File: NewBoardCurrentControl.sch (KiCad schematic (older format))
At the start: 21 parts, among them Q401 RSR030N06TL, U401 ADA4528-2ACPZ-RL, U402 782853152_WE-CBA_08

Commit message: add footprints julia
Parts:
- Q401: footprint SOT95P280X100-3N -> footprint libraries:RSR030N06TL
- U401: footprint CP_8_11_ADI -> footprint libraries:ADA4528-2ACPZ-RL
- U402: footprint (none) -> footprint libraries:782853121
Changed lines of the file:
@@
 F 0 "U401" H 5300 3937 60  0000 C CNN
 F 1 "ADA4528-2ACPZ-RL" H 5300 3831 60  0000 C CNN
-F 2 "CP_8_11_ADI" H 5300 3790 60  0001 C CNN
+F 2 "footprint libraries:ADA4528-2ACPZ-RL" H 5300 3790 60  0001 C CNN
 F 3 "" H 4500 3550 60  0000 C CNN
 	1    4500 3550
@@
 F 0 "Q401" H 7400 4615 50  0000 C CNN
 F 1 "RSR030N06TL" H 7400 4524 50  0000 C CNN
-F 2 "SOT95P280X100-3N" H 7900 4450 50  0001 L CNN
+F 2 "footprint libraries:RSR030N06TL" H 7900 4450 50  0001 L CNN
 F 3 "https://componentsearchengine.com/Datasheets/2/RSR030N06TL.pdf" H 7900 4350 50  0001 L CNN
 F 4 "Rohm, MOSFET, RSR030N06TL ROHM RSR030N06TL N-channel MOSFET Transistor, 3 A, 60 V, 3-Pin SC-96" H 7900 4250 50  0001 L CNN "Description"
@@
 F 0 "U402" V 7979 3528 50  0000 L CNN
 F 1 "782853152_WE-CBA_08" V 8070 3528 50  0000 L CNN
-F 2 "" H 8150 3400 50  0001 C CNN
+F 2 "footprint libraries:782853121" H 8150 3400 50  0001 C CNN
 F 3 "" H 8150 3400 50  0001 C CNN
 	1    8050 3400

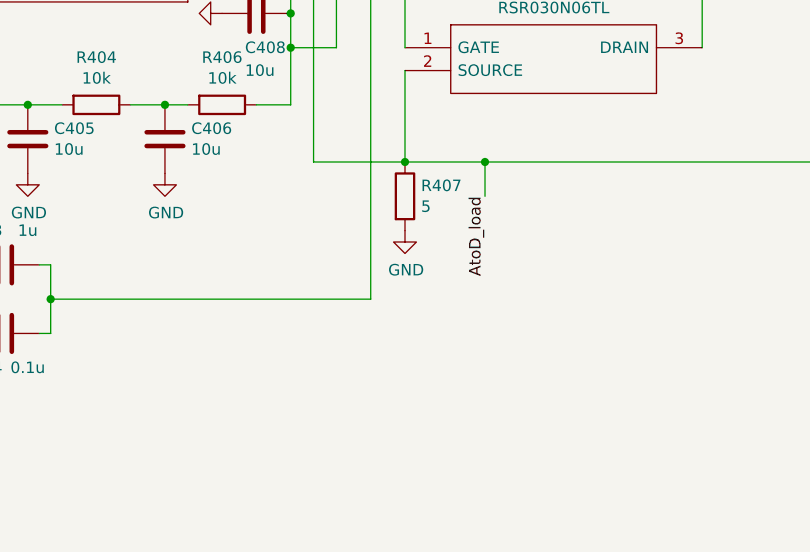
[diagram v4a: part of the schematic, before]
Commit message: added vishay dude & capacitor & resistor footprints
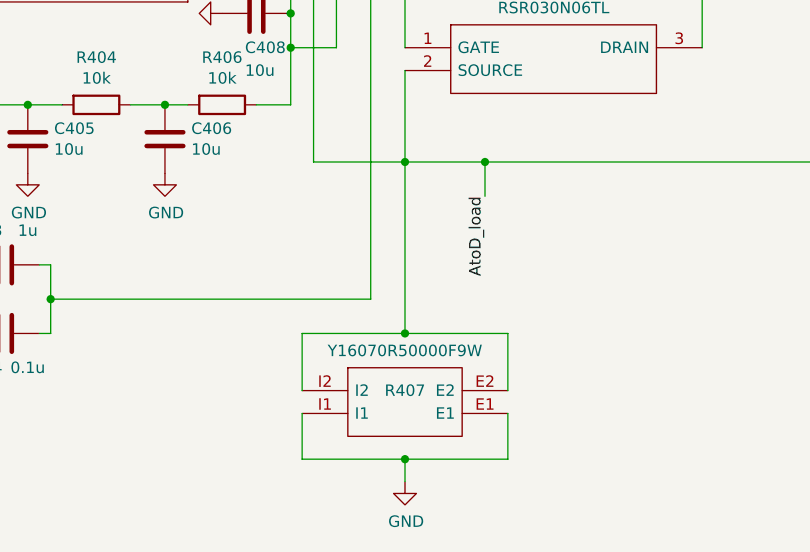
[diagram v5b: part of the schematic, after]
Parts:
- removed R407: 5, symbol Device:R
- added R407: Y16070R50000F9W, Y16072R00000T9W, symbol Y16070R50000F9W:Y16070R50000F9W
- C401, C402, C403, C404, C405, C406, C407, C408, C409, C410, C411: footprint (none) -> Capacitor_SMD:C_0402_1005Metric
- R401, R402, R405: footprint (none) -> Resistor_SMD:R_0402_1005Metric
- R403, R404, R406: footprint (none) -> Resistor_SMD:R_0603_1608Metric
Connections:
- net AtoD_load: now also R407.E2, R407.I2
- net GND: now also R407.E1, R407.I1
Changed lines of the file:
@@
 F 0 "C410" H 7615 2796 50  0000 L CNN
 F 1 "10u" H 7615 2705 50  0000 L CNN
-F 2 "" H 7538 2600 50  0001 C CNN
+F 2 "Capacitor_SMD:C_0402_1005Metric" H 7538 2600 50  0001 C CNN
 F 3 "~" H 7500 2750 50  0001 C CNN
 	1    7500 2750
@@
 F 0 "C411" H 9465 2796 50  0000 L CNN
 F 1 "10u" H 9465 2705 50  0000 L CNN
-F 2 "" H 9388 2600 50  0001 C CNN
+F 2 "Capacitor_SMD:C_0402_1005Metric" H 9388 2600 50  0001 C CNN
 F 3 "~" H 9350 2750 50  0001 C CNN
 	1    9350 2750
@@
 Connection ~ 6750 4850
 $Comp
-L Device:R R407
-U 1 1 60C96966
-P 6750 5000
-F 0 "R407" H 6820 5046 50  0000 L CNN
-F 1 "5" H 6820 4955 50  0000 L CNN
-F 2 "" V 6680 5000 50  0001 C CNN
-F 3 "~" H 6750 5000 50  0001 C CNN
-	1    6750 5000
-	1    0    0    -1
-$EndComp
-$Comp
 L power:GND #PWR0407
 U 1 1 60C97896
-P 6750 5150
-F 0 "#PWR0407" H 6750 4900 50  0001 C CNN
-F 1 "GND" H 6755 4977 50  0000 C CNN
-F 2 "" H 6750 5150 50  0001 C CNN
-F 3 "" H 6750 5150 50  0001 C CNN
-	1    6750 5150
+P 6750 6250
+F 0 "#PWR0407" H 6750 6000 50  0001 C CNN
+F 1 "GND" H 6755 6077 50  0000 C CNN
+F 2 "" H 6750 6250 50  0001 C CNN
+F 3 "" H 6750 6250 50  0001 C CNN
+	1    6750 6250
 	1    0    0    -1
 $EndComp
@@
 F 0 "R406" V 5743 4600 50  0000 C CNN
 F 1 "10k" V 5834 4600 50  0000 C CNN
-F 2 "" V 5880 4600 50  0001 C CNN
+F 2 "Resistor_SMD:R_0603_1608Metric" V 5880 4600 50  0001 C CNN
 F 3 "~" H 5950 4600 50  0001 C CNN
 	1    5950 4600
@@
 F 0 "C406" H 5815 4796 50  0000 L CNN
 F 1 "10u" H 5815 4705 50  0000 L CNN
-F 2 "" H 5738 4600 50  0001 C CNN
+F 2 "Capacitor_SMD:C_0402_1005Metric" H 5738 4600 50  0001 C CNN
 F 3 "~" H 5700 4750 50  0001 C CNN
 	1    5700 4750
@@
 F 0 "R404" V 5193 4600 50  0000 C CNN
 F 1 "10k" V 5284 4600 50  0000 C CNN
-F 2 "" V 5330 4600 50  0001 C CNN
+F 2 "Resistor_SMD:R_0603_1608Metric" V 5330 4600 50  0001 C CNN
 F 3 "~" H 5400 4600 50  0001 C CNN
 	1    5400 4600
@@
 F 0 "C405" H 5215 4796 50  0000 L CNN
 F 1 "10u" H 5215 4705 50  0000 L CNN
-F 2 "" H 5138 4600 50  0001 C CNN
+F 2 "Capacitor_SMD:C_0402_1005Metric" H 5138 4600 50  0001 C CNN
 F 3 "~" H 5100 4750 50  0001 C CNN
 	1    5100 4750
@@
 F 0 "R403" V 4593 4600 50  0000 C CNN
 F 1 "10k" V 4684 4600 50  0000 C CNN
-F 2 "" V 4730 4600 50  0001 C CNN
+F 2 "Resistor_SMD:R_0603_1608Metric" V 4730 4600 50  0001 C CNN
 F 3 "~" H 4800 4600 50  0001 C CNN
 	1    4800 4600
@@
 F 0 "C408" V 6250 4150 50  0000 L CNN
 F 1 "10u" V 6350 4150 50  0000 L CNN
-F 2 "" H 6138 4050 50  0001 C CNN
+F 2 "Capacitor_SMD:C_0402_1005Metric" H 6138 4050 50  0001 C CNN
 F 3 "~" H 6100 4200 50  0001 C CNN
 	1    6100 4200
@@
 F 0 "R401" V 3843 3650 50  0000 C CNN
 F 1 "1k" V 3934 3650 50  0000 C CNN
-F 2 "" V 3980 3650 50  0001 C CNN
+F 2 "Resistor_SMD:R_0402_1005Metric" V 3980 3650 50  0001 C CNN
 F 3 "~" H 4050 3650 50  0001 C CNN
 	1    4050 3650
@@
 F 0 "C401" V 3498 3650 50  0000 C CNN
 F 1 "1u" V 3589 3650 50  0000 C CNN
-F 2 "" H 3788 3500 50  0001 C CNN
+F 2 "Capacitor_SMD:C_0402_1005Metric" H 3788 3500 50  0001 C CNN
 F 3 "~" H 3750 3650 50  0001 C CNN
 	1    3750 3650
@@
 F 0 "R402" V 4557 3400 50  0000 C CNN
 F 1 "1k" V 4466 3400 50  0000 C CNN
-F 2 "" V 4280 3400 50  0001 C CNN
+F 2 "Resistor_SMD:R_0402_1005Metric" V 4280 3400 50  0001 C CNN
 F 3 "~" H 4350 3400 50  0001 C CNN
 	1    4350 3400
@@
 F 0 "C407" H 6015 2746 50  0000 L CNN
 F 1 "0.1u" H 6015 2655 50  0000 L CNN
-F 2 "" H 5938 2550 50  0001 C CNN
+F 2 "Capacitor_SMD:C_0402_1005Metric" H 5938 2550 50  0001 C CNN
 F 3 "~" H 5900 2700 50  0001 C CNN
 	1    5900 2700
@@
 F 0 "R405" V 5707 2850 50  0000 C CNN
 F 1 "100" V 5616 2850 50  0000 C CNN
-F 2 "" V 5430 2850 50  0001 C CNN
+F 2 "Resistor_SMD:R_0402_1005Metric" V 5430 2850 50  0001 C CNN
 F 3 "~" H 5500 2850 50  0001 C CNN
 	1    5500 2850
@@
 F 0 "C409" H 6565 3246 50  0000 L CNN
 F 1 "1u" H 6565 3155 50  0000 L CNN
-F 2 "" H 6488 3050 50  0001 C CNN
+F 2 "Capacitor_SMD:C_0402_1005Metric" H 6488 3050 50  0001 C CNN
 F 3 "~" H 6450 3200 50  0001 C CNN
 	1    6450 3200
@@
 F 0 "C402" H 3735 4154 50  0000 R CNN
 F 1 "0.1u" H 3735 4245 50  0000 R CNN
-F 2 "" H 3888 4050 50  0001 C CNN
+F 2 "Capacitor_SMD:C_0402_1005Metric" H 3888 4050 50  0001 C CNN
 F 3 "~" H 3850 4200 50  0001 C CNN
 	1    3850 4200
@@
 F 0 "C403" V 4850 5200 50  0000 C CNN
 F 1 "1u" V 4850 5400 50  0000 C CNN
-F 2 "" H 5038 5150 50  0001 C CNN
+F 2 "Capacitor_SMD:C_0402_1005Metric" H 5038 5150 50  0001 C CNN
 F 3 "~" H 5000 5300 50  0001 C CNN
 	1    5000 5300
@@
 F 0 "C404" V 5150 5500 50  0000 C CNN
 F 1 "0.1u" V 5150 5700 50  0000 C CNN
-F 2 "" H 5038 5450 50  0001 C CNN
+F 2 "Capacitor_SMD:C_0402_1005Metric" H 5038 5450 50  0001 C CNN
 F 3 "~" H 5000 5600 50  0001 C CNN
 	1    5000 5600
@@
 Text Label 7650 1450 2    50   ~ 0
 V2_3.3V
+$Comp
+L Y16070R50000F9W:Y16070R50000F9W R407
+U 1 1 60D382BE
+P 6300 5850
+F 0 "R407" H 6750 5850 50  0000 C CNN
+F 1 "Y16070R50000F9W" H 6750 6024 50  0000 C CNN
+F 2 "Y16072R00000T9W" H 7050 5950 50  0001 L CNN
+F 3 "http://www.vishaypg.com/docs/63094/vcs1625z.pdf" H 7050 5850 50  0001 L CNN
+F 4 "Vishay Foil Resistors VCS Series Metal Foil Precision Surface Mount Fixed Resistor 500m +/-1% 0.5W +/-0.2ppm/C" H 7050 5750 50  0001 L CNN "Description"
+F 5 "1" H 7050 5650 50  0001 L CNN "Height"
+F 6 "Vishay" H 7050 5550 50  0001 L CNN "Manufacturer_Name"
+F 7 "Y16070R50000F9W" H 7050 5450 50  0001 L CNN "Manufacturer_Part_Number"
+F 8 "71-VCS1625Z0R5000FSW" H 7050 5350 50  0001 L CNN "Mouser Part Number"
+F 9 "https://www.mouser.co.uk/ProductDetail/Vishay-Precision-Group-Foil-Resistors/Y16070R50000F9W?qs=adduyb8LSTEElqj6iywYlw%3D%3D" H 7050 5250 50  0001 L CNN "Mouser Price/Stock"
+F 10 "Y16070R50000F9W" H 7050 5150 50  0001 L CNN "Arrow Part Number"
+F 11 "https://www.arrow.com/en/products/y16070r50000f9w/vishay-precision-group" H 7050 5050 50  0001 L CNN "Arrow Price/Stock"
+	1    6300 5850
+	1    0    0    -1
+$EndComp
+Wire Wire Line
+	6750 5600 6300 5600
+Wire Wire Line
+	6300 5600 6300 5850
+Wire Wire Line
+	6750 4850 6750 5600
+Wire Wire Line
+	7200 5850 7200 5600
+Wire Wire Line
+	7200 5600 6750 5600
+Connection ~ 6750 5600
+Wire Wire Line
+	7200 5950 7200 6150
+Wire Wire Line
+	7200 6150 6750 6150
+Wire Wire Line
+	6750 6150 6750 6250
+Wire Wire Line
+	6750 6150 6300 6150
+Wire Wire Line
+	6300 6150 6300 5950
+Connection ~ 6750 6150
 $EndSCHEMATC

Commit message: changed all 'odd' resistors in thermal control footprints
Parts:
- R407: footprint Y16072R00000T9W -> footprint libraries:Y16072R00000T9W
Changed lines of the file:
@@
 F 0 "R407" H 6750 5850 50  0000 C CNN
 F 1 "Y16070R50000F9W" H 6750 6024 50  0000 C CNN
-F 2 "Y16072R00000T9W" H 7050 5950 50  0001 L CNN
+F 2 "footprint libraries:Y16072R00000T9W" H 7050 5950 50  0001 L CNN
 F 3 "http://www.vishaypg.com/docs/63094/vcs1625z.pdf" H 7050 5850 50  0001 L CNN
 F 4 "Vishay Foil Resistors VCS Series Metal Foil Precision Surface Mount Fixed Resistor 500m +/-1% 0.5W +/-0.2ppm/C" H 7050 5750 50  0001 L CNN "Description"

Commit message: changes on nano and laser
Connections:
- net V2_3.3V renamed Laser_3.3VPower_Supply
- net Laser_3.3VPower_Supply: no longer C410.2, U402.~
- new net To_Laser: C410.2, U402.~
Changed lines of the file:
@@
 	7500 2900 7500 3050
-Wire Wire Line
-	8050 2200 8050 3050
 Wire Wire Line
 	9350 2900 9350 3700
@@
 Text Label 4250 4200 0    50   ~ 0
 V5
-Connection ~ 8050 3050
 Connection ~ 8050 3700
 $Comp
@@
 	6300 6150 6300 5950
 Connection ~ 6750 6150
+Wire Wire Line
+	8050 2200 8050 2450
+Wire Wire Line
+	8050 2450 8500 2450
+Wire Wire Line
+	8500 2450 8500 1500
+Wire Wire Line
+	8500 1500 10500 1500
+Wire Wire Line
+	8050 3050 8050 2900
+Wire Wire Line
+	8050 2900 8850 2900
+Wire Wire Line
+	8850 2900 8850 1900
+Wire Wire Line
+	8850 1900 10500 1900
+Connection ~ 8050 3050
+Text Label 10500 1500 2    50   ~ 0
+Laser_3.3VPower_Supply
+Text Label 10500 1900 2    50   ~ 0
+To_Laser
 $EndSCHEMATC

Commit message: mod signal
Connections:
- net SINE(0_0_10k)V3 renamed MODULATION_SIGNAL
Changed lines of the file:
@@
 $EndComp
 Text Label 3600 3850 2    50   ~ 0
-SINE(0_0_10k)V3
+MODULATION_SIGNAL
 Wire Wire Line
 	3600 3650 3600 3850
